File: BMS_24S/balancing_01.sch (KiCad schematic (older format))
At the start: 61 parts, among them Q2701 Si2302DS, Q2702 Si2302DS, Q2703 Si2302DS, Q2704 Si2302DS, U2701 TLP290-4

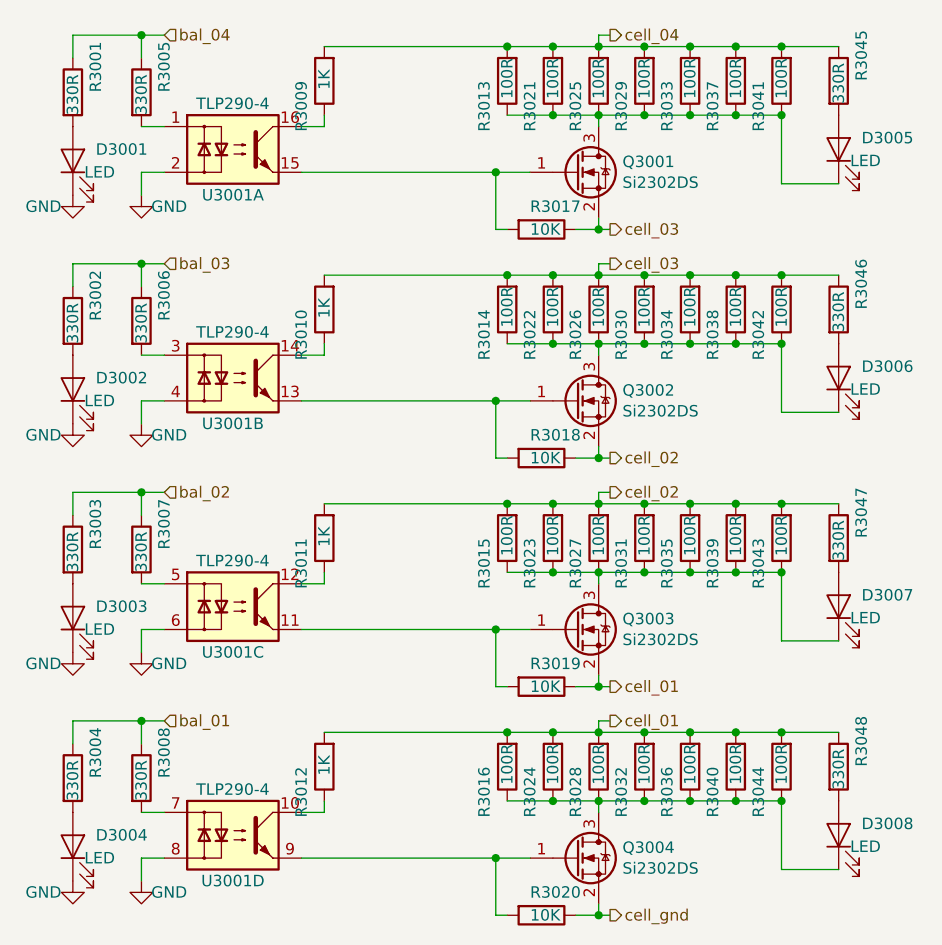
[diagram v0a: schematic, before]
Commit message: update balancing circuit
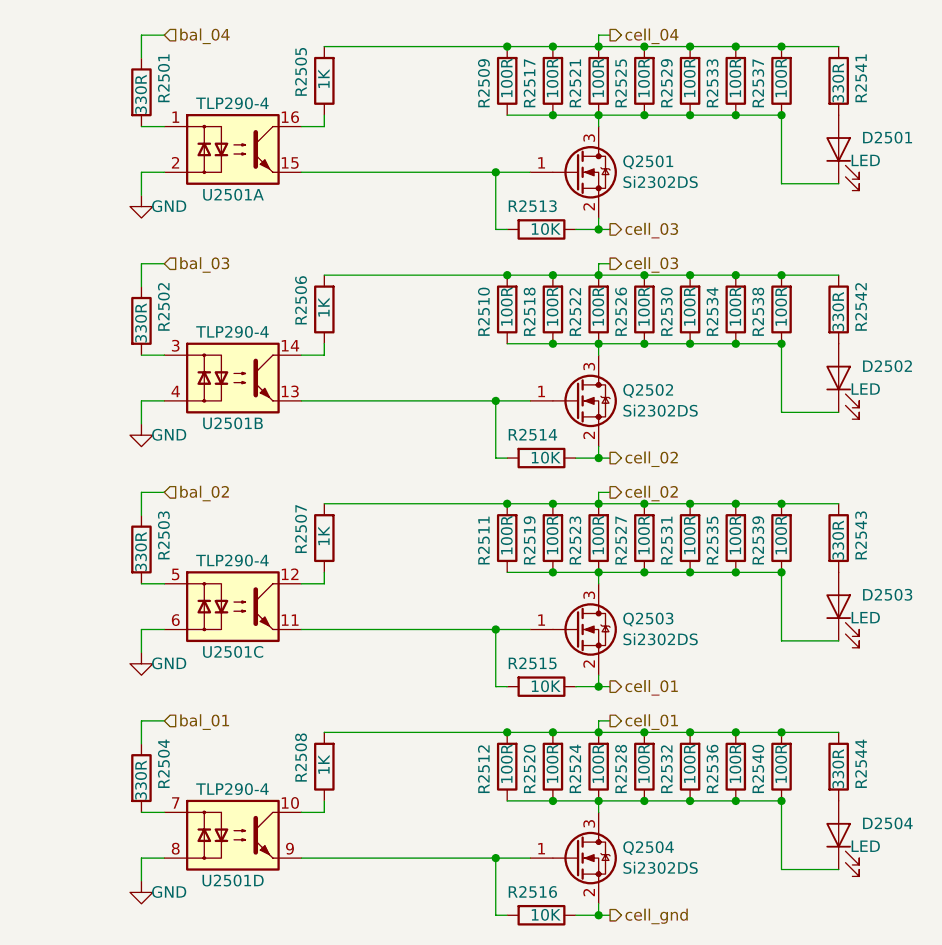
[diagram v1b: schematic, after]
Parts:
- removed D2701, D2702, D2703, D2704: LED, e-Power:LED_0805_1.15x1.40mm_HandSolder, symbol e-Power:LED
- removed R2701, R2702, R2703, R2704: 330R, Resistor_SMD:R_0805_2012Metric, symbol Device:R
- R2505: renamed from R2709; LCSC (none) -> C17513; Power (none) -> 1/8W; Precision (none) -> 1%; Voltage (none) -> 150V
- R2506: renamed from R2710; LCSC (none) -> C17513; Power (none) -> 1/8W; Precision (none) -> 1%; Voltage (none) -> 150V
- R2507: renamed from R2711; LCSC (none) -> C17513; Power (none) -> 1/8W; Precision (none) -> 1%; Voltage (none) -> 150V
- R2508: renamed from R2712; LCSC (none) -> C17513; Power (none) -> 1/8W; Precision (none) -> 1%; Voltage (none) -> 150V
- R2513: renamed from R2717; LCSC (none) -> C17414; Power (none) -> 1/8W; Precision (none) -> 1%; Voltage (none) -> 150V
- R2514: renamed from R2718; LCSC (none) -> C17414; Power (none) -> 1/8W; Precision (none) -> 1%; Voltage (none) -> 150V
- R2515: renamed from R2719; LCSC (none) -> C17414; Power (none) -> 1/8W; Precision (none) -> 1%; Voltage (none) -> 150V
- R2516: renamed from R2720; LCSC (none) -> C17414; Power (none) -> 1/8W; Precision (none) -> 1%; Voltage (none) -> 150V
- renumbered D2705 to D2501, D2706 to D2502, D2707 to D2503, D2708 to D2504, Q2701 to Q2501, Q2702 to Q2502, Q2703 to Q2503, Q2704 to Q2504, R2705 to R2501, R2706 to R2502, R2707 to R2503, R2708 to R2504, R2713 to R2509, R2714 to R2510, R2715 to R2511, R2716 to R2512, R2721 to R2517, R2722 to R2518, R2723 to R2519, R2724 to R2520, R2725 to R2521, R2726 to R2522, R2727 to R2523, R2728 to R2524, R2729 to R2525, R2730 to R2526, R2731 to R2527, R2732 to R2528, R2733 to R2529, R2734 to R2530, R2735 to R2531, R2736 to R2532, R2737 to R2533, R2738 to R2534, R2739 to R2535, R2740 to R2536, R2741 to R2537, R2742 to R2538, R2743 to R2539, R2744 to R2540, R2745 to R2541, R2746 to R2542, R2747 to R2543, R2748 to R2544, U2701 to U2501

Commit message: updates made on BMS
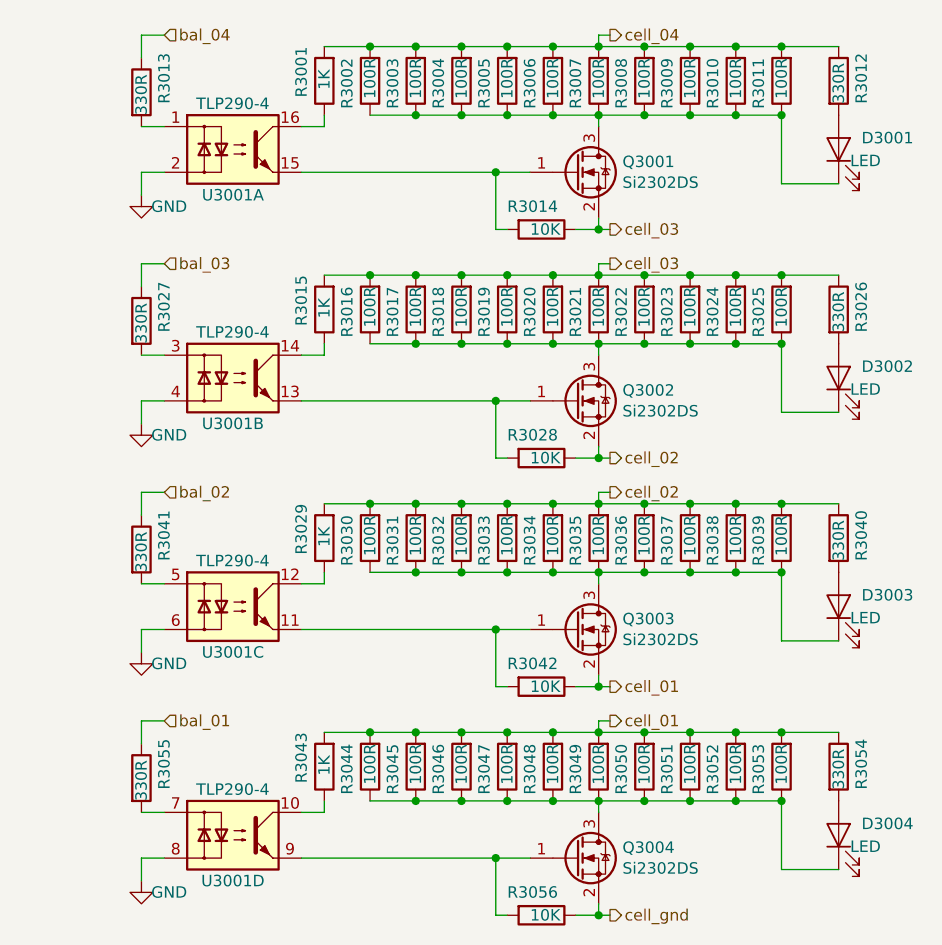
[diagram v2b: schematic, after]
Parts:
- added R2502, R2503, R2504, R2516, R2517, R2518, R2530, R2531, R2532, R2544, R2545, R2546: 100R, Resistor_SMD:R_2512_6332Metric, symbol Device:R
- renumbered R2505 to R2501, R2509 to R2505, R2517 to R2506, R2521 to R2507, R2525 to R2508, R2529 to R2509, R2533 to R2510, R2537 to R2511, R2541 to R2512, R2501 to R2513, R2513 to R2514, R2506 to R2515, R2510 to R2519, R2518 to R2520, R2522 to R2521, R2526 to R2522, R2530 to R2523, R2534 to R2524, R2538 to R2525, R2542 to R2526, R2502 to R2527, R2514 to R2528, R2507 to R2529, R2511 to R2533, R2519 to R2534, R2523 to R2535, R2527 to R2536, R2531 to R2537, R2535 to R2538, R2543 to R2540, R2503 to R2541, R2515 to R2542, R2508 to R2543, R2512 to R2547, R2520 to R2548, R2524 to R2549, R2528 to R2550, R2532 to R2551, R2536 to R2552, R2540 to R2553, R2544 to R2554, R2504 to R2555, R2516 to R2556
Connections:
- net cell_01: now also R2544.2, R2545.2, R2546.2
- net cell_02: now also R2530.2, R2531.2, R2532.2
- net cell_03: now also R2516.2, R2517.2, R2518.2
- net cell_04: now also R2502.2, R2503.2, R2504.2
- net at D2504.1 (K), Q2504.3 (D), R2547.1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: now also R2544.1, R2545.1, R2546.1
- net at D2503.1 (K), Q2503.3 (D), R2533.1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: now also R2530.1, R2531.1, R2532.1
- net at D2502.1 (K), Q2502.3 (D), R2519.1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: now also R2516.1, R2517.1, R2518.1
- net at D2501.1 (K), Q2501.3 (D), R2505.1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: now also R2502.1, R2503.1, R2504.1

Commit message: update all circuits
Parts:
- removed Q2501, Q2502, Q2503, Q2504: Si2302DS, Package_TO_SOT_SMD:SOT-23, symbol e-Power:Si2302DS
- added Q? (x4): Si2302DS, Package_TO_SOT_SMD:SOT-23, symbol e-Power:Si2302DS
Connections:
- net cell_01: now also Q?.2 (S)
- net cell_02: now also Q?.2 (S)
- net cell_03: now also Q?.2 (S)
- net cell_gnd: now also Q?.2 (S)
- net at R2556.2, U2501.9: now also Q?.1 (G)
- net at D2504.1 (K), R2544.1, R2545.1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: now also Q?.3 (D)
- net at R2542.2, U2501.11: now also Q?.1 (G)
- net at D2503.1 (K), R2530.1, R2531.1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: now also Q?.3 (D)
- net at R2528.2, U2501.13: now also Q?.1 (G)
- net at D2502.1 (K), R2516.1, R2517.1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: now also Q?.3 (D)
- net at R2514.2, U2501.15: now also Q?.1 (G)
- net at D2501.1 (K), R2502.1, R2503.1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: now also Q?.3 (D)

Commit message: get BSPD
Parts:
- gave numbers to parts that had none: 4

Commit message: update bms pcb
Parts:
- renumbered Q1 to Q2501, Q2 to Q2502, Q3 to Q2503, Q4 to Q2504
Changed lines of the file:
@@
 	4500 3950 4300 3950
 $Comp
-L e-Power:Si2302DS Q1
+L e-Power:Si2302DS Q2501
 U 1 1 5F341634
 P 5000 1200
-AR Path="/5F25407D/5F255A50/5F341634" Ref="Q1"  Part="1"
-AR Path="/5F25407D/5F34C39A/5F341634" Ref="Q5"  Part="1"
-AR Path="/5F25407D/5F34DE6D/5F341634" Ref="Q9"  Part="1"
-AR Path="/5F25407D/5F352741/5F341634" Ref="Q13"  Part="1"
-AR Path="/5F25407D/5F7CE31F/5F341634" Ref="Q17"  Part="1"
-AR Path="/5F25407D/5F7CF78E/5F341634" Ref="Q21"  Part="1"
-F 0 "Q21" H 5204 1246 50  0000 L CNN
+AR Path="/5F25407D/5F255A50/5F341634" Ref="Q2501"  Part="1"
+AR Path="/5F25407D/5F34C39A/5F341634" Ref="Q2601"  Part="1"
+AR Path="/5F25407D/5F34DE6D/5F341634" Ref="Q2701"  Part="1"
+AR Path="/5F25407D/5F352741/5F341634" Ref="Q2801"  Part="1"
+AR Path="/5F25407D/5F7CE31F/5F341634" Ref="Q2901"  Part="1"
+AR Path="/5F25407D/5F7CF78E/5F341634" Ref="Q3001"  Part="1"
+F 0 "Q3001" H 5204 1246 50  0000 L CNN
 F 1 "Si2302DS" H 5204 1155 50  0000 L CNN
 F 2 "Package_TO_SOT_SMD:SOT-23" H 5200 1125 50  0001 L CIN
@@
 $EndComp
 $Comp
-L e-Power:Si2302DS Q2
+L e-Power:Si2302DS Q2502
 U 1 1 5F34235C
 P 5000 2200
-AR Path="/5F25407D/5F255A50/5F34235C" Ref="Q2"  Part="1"
-AR Path="/5F25407D/5F34C39A/5F34235C" Ref="Q6"  Part="1"
-AR Path="/5F25407D/5F34DE6D/5F34235C" Ref="Q10"  Part="1"
-AR Path="/5F25407D/5F352741/5F34235C" Ref="Q14"  Part="1"
-AR Path="/5F25407D/5F7CE31F/5F34235C" Ref="Q18"  Part="1"
-AR Path="/5F25407D/5F7CF78E/5F34235C" Ref="Q22"  Part="1"
-F 0 "Q22" H 5204 2246 50  0000 L CNN
+AR Path="/5F25407D/5F255A50/5F34235C" Ref="Q2502"  Part="1"
+AR Path="/5F25407D/5F34C39A/5F34235C" Ref="Q2602"  Part="1"
+AR Path="/5F25407D/5F34DE6D/5F34235C" Ref="Q2702"  Part="1"
+AR Path="/5F25407D/5F352741/5F34235C" Ref="Q2802"  Part="1"
+AR Path="/5F25407D/5F7CE31F/5F34235C" Ref="Q2902"  Part="1"
+AR Path="/5F25407D/5F7CF78E/5F34235C" Ref="Q3002"  Part="1"
+F 0 "Q3002" H 5204 2246 50  0000 L CNN
 F 1 "Si2302DS" H 5204 2155 50  0000 L CNN
 F 2 "Package_TO_SOT_SMD:SOT-23" H 5200 2125 50  0001 L CIN
@@
 $EndComp
 $Comp
-L e-Power:Si2302DS Q3
+L e-Power:Si2302DS Q2503
 U 1 1 5F3428FA
 P 5000 3200
-AR Path="/5F25407D/5F255A50/5F3428FA" Ref="Q3"  Part="1"
-AR Path="/5F25407D/5F34C39A/5F3428FA" Ref="Q7"  Part="1"
-AR Path="/5F25407D/5F34DE6D/5F3428FA" Ref="Q11"  Part="1"
-AR Path="/5F25407D/5F352741/5F3428FA" Ref="Q15"  Part="1"
-AR Path="/5F25407D/5F7CE31F/5F3428FA" Ref="Q19"  Part="1"
-AR Path="/5F25407D/5F7CF78E/5F3428FA" Ref="Q23"  Part="1"
-F 0 "Q23" H 5204 3246 50  0000 L CNN
+AR Path="/5F25407D/5F255A50/5F3428FA" Ref="Q2503"  Part="1"
+AR Path="/5F25407D/5F34C39A/5F3428FA" Ref="Q2603"  Part="1"
+AR Path="/5F25407D/5F34DE6D/5F3428FA" Ref="Q2703"  Part="1"
+AR Path="/5F25407D/5F352741/5F3428FA" Ref="Q2803"  Part="1"
+AR Path="/5F25407D/5F7CE31F/5F3428FA" Ref="Q2903"  Part="1"
+AR Path="/5F25407D/5F7CF78E/5F3428FA" Ref="Q3003"  Part="1"
+F 0 "Q3003" H 5204 3246 50  0000 L CNN
 F 1 "Si2302DS" H 5204 3155 50  0000 L CNN
 F 2 "Package_TO_SOT_SMD:SOT-23" H 5200 3125 50  0001 L CIN
@@
 $EndComp
 $Comp
-L e-Power:Si2302DS Q4
+L e-Power:Si2302DS Q2504
 U 1 1 5F3433A2
 P 5000 4200
-AR Path="/5F25407D/5F255A50/5F3433A2" Ref="Q4"  Part="1"
-AR Path="/5F25407D/5F34C39A/5F3433A2" Ref="Q8"  Part="1"
-AR Path="/5F25407D/5F34DE6D/5F3433A2" Ref="Q12"  Part="1"
-AR Path="/5F25407D/5F352741/5F3433A2" Ref="Q16"  Part="1"
-AR Path="/5F25407D/5F7CE31F/5F3433A2" Ref="Q20"  Part="1"
-AR Path="/5F25407D/5F7CF78E/5F3433A2" Ref="Q24"  Part="1"
-F 0 "Q24" H 5204 4246 50  0000 L CNN
+AR Path="/5F25407D/5F255A50/5F3433A2" Ref="Q2504"  Part="1"
+AR Path="/5F25407D/5F34C39A/5F3433A2" Ref="Q2604"  Part="1"
+AR Path="/5F25407D/5F34DE6D/5F3433A2" Ref="Q2704"  Part="1"
+AR Path="/5F25407D/5F352741/5F3433A2" Ref="Q2804"  Part="1"
+AR Path="/5F25407D/5F7CE31F/5F3433A2" Ref="Q2904"  Part="1"
+AR Path="/5F25407D/5F7CF78E/5F3433A2" Ref="Q3004"  Part="1"
+F 0 "Q3004" H 5204 4246 50  0000 L CNN
 F 1 "Si2302DS" H 5204 4155 50  0000 L CNN
 F 2 "Package_TO_SOT_SMD:SOT-23" H 5200 4125 50  0001 L CIN

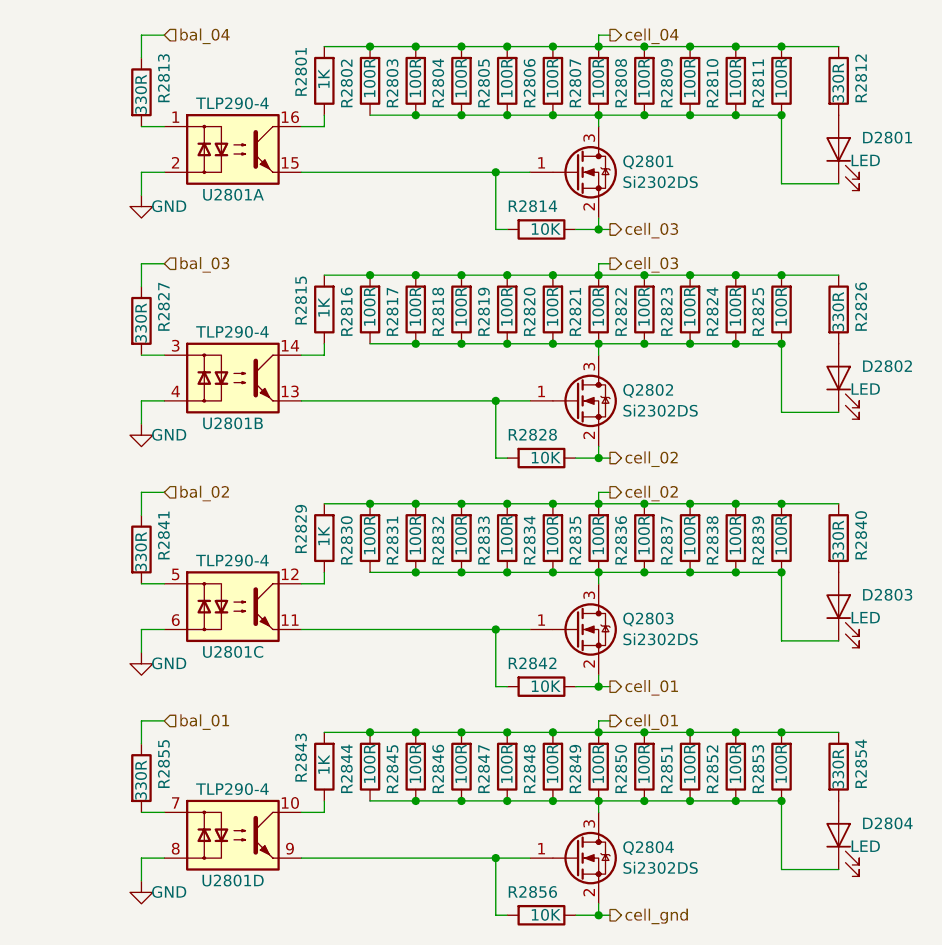
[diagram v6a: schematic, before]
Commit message: updates made on BMS
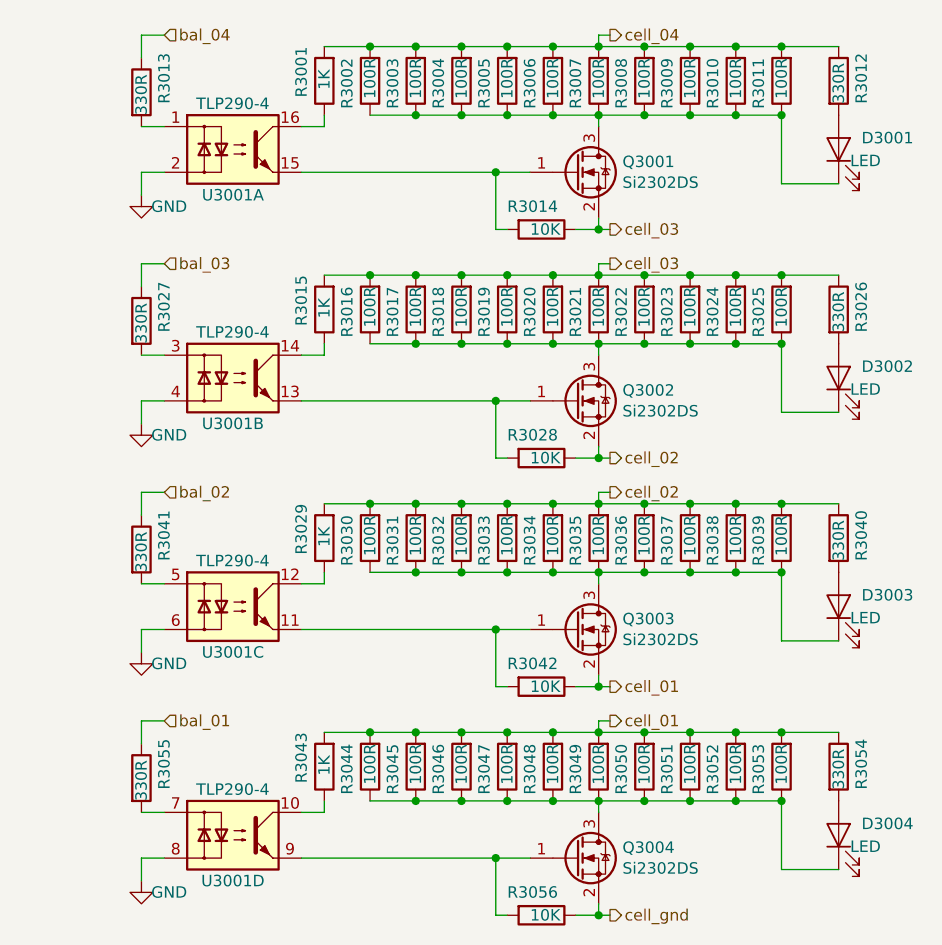
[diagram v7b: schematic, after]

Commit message: updates made on bms, almost done
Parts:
- U2501: LCSC (none) -> C39031
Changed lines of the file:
@@
 $Descr User 7087 6299
 encoding utf-8
-Sheet 28 31
+Sheet 29 31
 Title ""
 Date "2020-04-26"
@@
 F 2 "e-Power:SOIC-16_4.55x10.3mm_P1.27mm(TLP290-4)" H 2650 2900 50  0001 L CIN
 F 3 "https://toshiba.semicon-storage.com/info/docget.jsp?did=12855&prodName=TLP290-4" H 3525 3100 50  0001 L CNN
+F 4 "C39031" H 3500 3100 50  0001 C CNN "LCSC"
 	3    3500 3100
 	1    0    0    -1
@@
 F 2 "e-Power:SOIC-16_4.55x10.3mm_P1.27mm(TLP290-4)" H 2650 900 50  0001 L CIN
 F 3 "https://toshiba.semicon-storage.com/info/docget.jsp?did=12855&prodName=TLP290-4" H 3525 1100 50  0001 L CNN
+F 4 "C39031" H 3500 1100 50  0001 C CNN "LCSC"
 	1    3500 1100
 	1    0    0    -1
@@
 F 2 "e-Power:SOIC-16_4.55x10.3mm_P1.27mm(TLP290-4)" H 2650 1900 50  0001 L CIN
 F 3 "https://toshiba.semicon-storage.com/info/docget.jsp?did=12855&prodName=TLP290-4" H 3525 2100 50  0001 L CNN
+F 4 "C39031" H 3500 2100 50  0001 C CNN "LCSC"
 	2    3500 2100
 	1    0    0    -1
@@
 F 2 "e-Power:SOIC-16_4.55x10.3mm_P1.27mm(TLP290-4)" H 2650 3900 50  0001 L CIN
 F 3 "https://toshiba.semicon-storage.com/info/docget.jsp?did=12855&prodName=TLP290-4" H 3525 4100 50  0001 L CNN
+F 4 "C39031" H 3500 4100 50  0001 C CNN "LCSC"
 	4    3500 4100
 	1    0    0    -1
